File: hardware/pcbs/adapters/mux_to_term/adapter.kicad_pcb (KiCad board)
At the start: 2 copper layers, 26.7 x 50.8 mm, 3 parts, among them K1 CONN_3, P1 CONN_5X2, P2 CONN_7

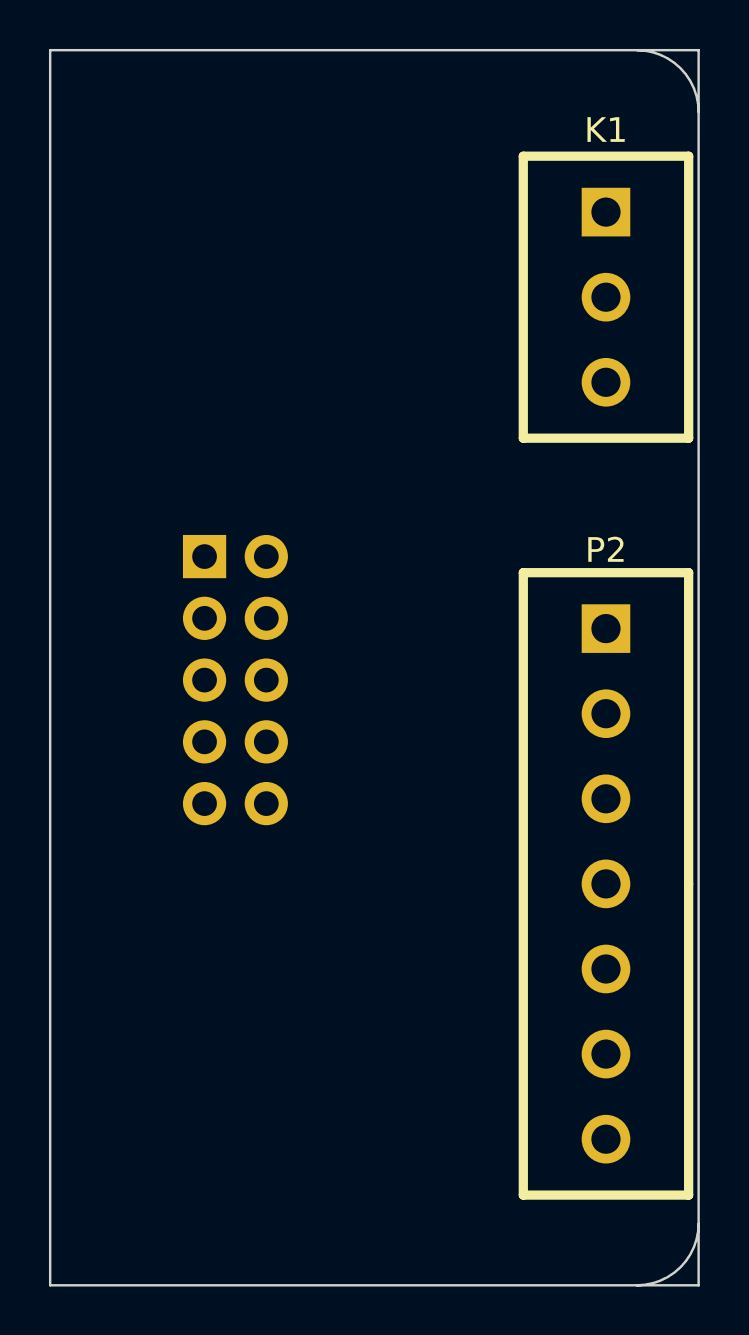
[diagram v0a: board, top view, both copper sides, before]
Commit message: Modified v0.2 of multiplexer. Extended tab with 5x2 header connector to deal with interference issue. Finished the two initial multiplexer adapter pcbs - mux_to_term and mux_to_3pin.
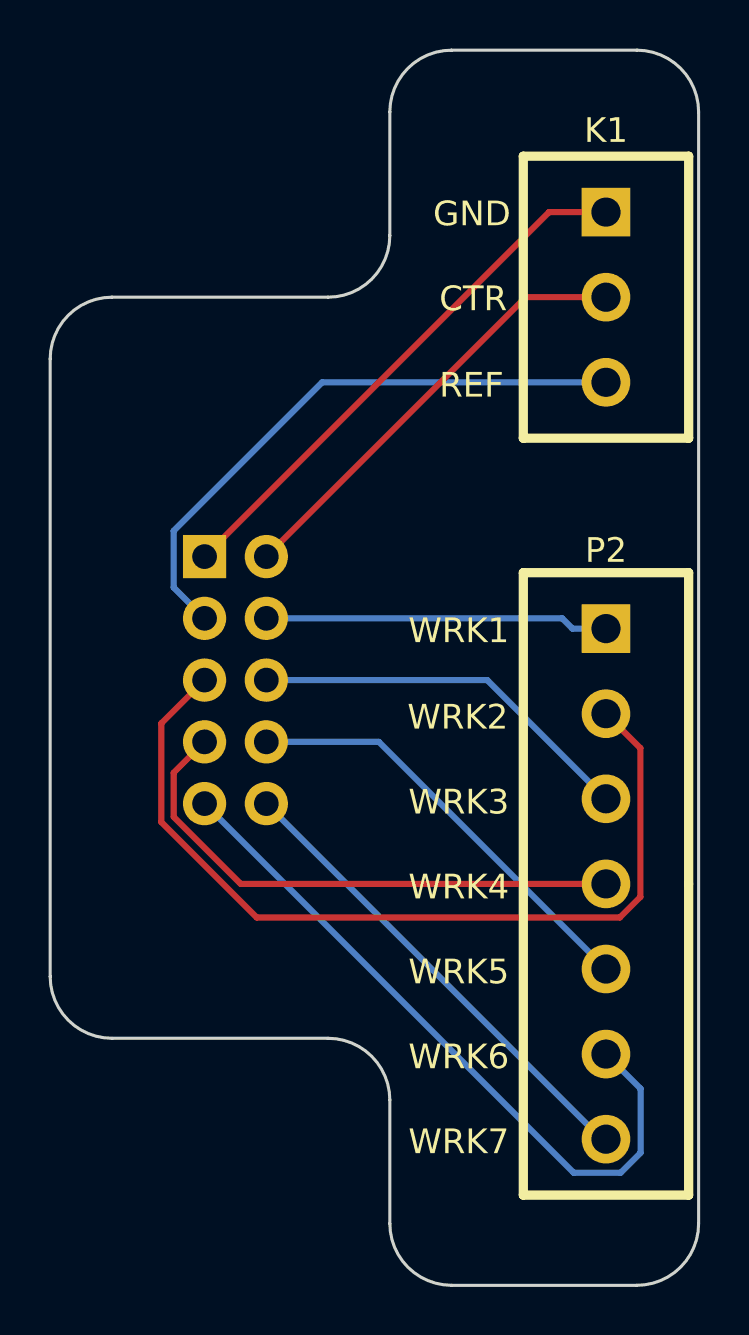
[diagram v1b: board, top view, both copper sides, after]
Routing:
- net /WRK_2: track 0.00 -> 36.4 mm
- net /WRK_6: track 0.00 -> 29.2 mm
- net /REF_SW: track 0.00 -> 24.4 mm
- net /WRK_4: track 0.00 -> 22.5 mm
- net /GND: track 0.00 -> 22.4 mm
- net /WRK_7: track 0.00 -> 19.7 mm
- net /CTR_SW: track 0.00 -> 18.4 mm
- net /WRK_5: track 0.00 -> 17.8 mm
- net /WRK_3: track 0.00 -> 16.0 mm
- net /WRK_1: track 0.00 -> 14.1 mm
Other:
- outline, holes or cut-outs redrawn
- board text added: "CTR"
- board text added: "GND"
- board text added: "REF"
- board text added: "Rodeostat Multiplexer Screw Terminal Adapter V0.1 R1 www.iorodeo.com"
- board text added: "WRK1"
- board text added: "WRK2"
- board text added: "WRK3"
- board text added: "WRK4"
- board text added: "WRK5"
- board text added: "WRK6"
- board text added: "WRK7"
